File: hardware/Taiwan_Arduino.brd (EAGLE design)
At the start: 97.2 x 35.7 mm, 44 parts, among them J1 AVR_SPI_PRG_62X3_LOCK, T1 2SC, T2 2N, U1 ATMEGA328P_PDIP, Y2 16mhz

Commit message: Ver 1.0
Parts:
- removed T1: 2SC, transistor:TO92-ECB
- moved JP3 2.50 mm to (87.4, 23.5), turned to 180 degrees
- moved C1 2.35 mm to (77.4, 20.8)
- moved T2 1.61 mm to (83.2, 19.7)
- moved R16 0.61 mm to (75.5, 13.0)
- moved TP6 0.30 mm to (63.2, 9.83)
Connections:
- removed net N$18: JP3.2, T1.C, T2.C
- new net N$12: JP3.1, T2.C
- net +5V: now also JP3.2; no longer JP3.1
- net GND: no longer T1.E
- net N$22: no longer T1.B
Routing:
- net N$12: track 0.00 -> 6.79 mm
- net N$18: track 6.31 -> 0.00 mm
- net +5V: track 140.1 -> 144.2 mm
- net N$22: track 19.2 -> 22.6 mm
- net N$17: track 47.1 -> 48.2 mm
- net N$11: track 76.6 -> 76.0 mm
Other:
- board size 97.2 x 35.7 mm -> 97.4 x 35.6 mm

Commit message: ver 1.0
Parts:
- removed R7: 1M, SparkFun-Resistors:AXIAL-0.4
- removed TP5: TEST-POINT, SparkFun-Passives:PADBIG
- removed U$1: SPI_FLASH-X25XX, SparkFun-DigitalIC:DIL08
- added D3: 3.3V, _JJG-parts:0204V
- added JP1: Battery, SparkFun-Connectors:1X02
- added U2: SPI_FLASH, SparkFun-DigitalIC:DIL08
- C10, C13, C5, C8: device SparkFun-Capacitors:CAP-PTH-SMALL -> SparkFun-Capacitors:CAP-PTH-5MM
- C2: value 0.1uf -> 104; device SparkFun-Capacitors:CAP-PTH-SMALL -> SparkFun-Capacitors:CAP-PTH-5MM
- JP3: value M02JST-PTH-VERT -> M021X02_NO_SILK; device SparkFun-Connectors:JST-2-PTH-VERT -> SparkFun-Connectors:1X02_NO_SILK
- R1: value (none) -> 10
- R9: device SparkFun-Resistors:AXIAL-0.4 -> SparkFun-Resistors:AXIAL-0.1
- T2: value 2N -> 2N2222
- moved R8 10.2 mm to (70.1, 13.6)
- moved R9 7.37 mm to (26.0, 22.2), turned to 90 degrees
- moved C2 5.72 mm to (47.4, 9.20)
- moved JP3 4.26 mm to (86.0, 19.5), turned to 90 degrees
- moved R6 4.24 mm to (26.0, 16.9)
- moved U1 4.01 mm to (45.3, 21.0)
- moved R5 3.64 mm to (72.8, 13.6), turned to 270 degrees
- moved R10 2.80 mm to (32.7, 27.4)
- moved TP3 2.73 mm to (81.9, 11.3)
- moved R13 2.72 mm to (36.4, 14.5)
- moved RV1 2.62 mm to (69.2, 20.5)
- moved R12 2.60 mm to (38.9, 14.6)
- moved R11 2.53 mm to (44.5, 11.8)
- moved R15 2.50 mm to (34.9, 27.4), turned to 90 degrees
- moved C5 2.33 mm to (25.7, 13.4), turned to 0 degrees
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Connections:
- removed net N$27: R7.P$2, TP5.P$1, U1.6
- new net N$18: D3.1, JP1.2
- net +5V: now also D3.2, U2.3, U2.7, U2.8; no longer U$1.3, U$1.7, U$1.8
- net GND: now also JP1.1, U2.4; no longer U$1.4
- net N$10: now also U2.2; no longer U$1.2
- net N$11: now also U1.26; no longer R7.P$1, U1.25
- net N$23: now also U2.5; no longer U$1.5
- net N$28: now also U1.16, U2.1; no longer U$1.1, U1.14
- net N$3: now also U1.14; no longer U1.16
- net N$5: now also U1.25; no longer U1.24
- net N$6: now also U2.6; no longer U$1.6
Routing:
- net N$27: track 27.5 -> 0.00 mm
- net +5V: track 144.2 -> 159.4 mm
- net 1: track 11.9 -> 17.9 mm
- net N$17: track 48.2 -> 42.8 mm
- net N$3: track 35.4 -> 39.9 mm, vias 0 -> 1
- net N$13: track 14.0 -> 10.0 mm
- net N$18: track 0.00 -> 3.71 mm
- net N$11: track 76.0 -> 79.2 mm
- net N$9: track 10.7 -> 13.5 mm
- net N$12: track 6.79 -> 4.01 mm
- net N$15: track 17.1 -> 19.6 mm
- net N$5: track 14.9 -> 12.4 mm
- net N$14: track 10.7 -> 13.1 mm
- net N$2: track 7.57 -> 5.53 mm
- net N$29: track 31.7 -> 33.6 mm
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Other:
- board text added: "+"
- board text added: "-"
- board text added: "104"
- board text added: "22pf"
- board text added: "Bat"
- board text added: "Reset"
- board text added: "台灣"

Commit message: add tag on IO
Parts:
- moved TP8 0.98 mm to (90.4, 16.8)
- moved R10 0.30 mm to (32.4, 27.4)
- moved R15 0.20 mm to (34.7, 27.4)
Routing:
- net N$17: track 42.8 -> 43.4 mm
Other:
- board text added: "A2"
- board text added: "A4"
- board text added: "A5"
- board text added: "D5"
- board text added: "D6"
- board text added: "D8"
- board text removed: "台灣"

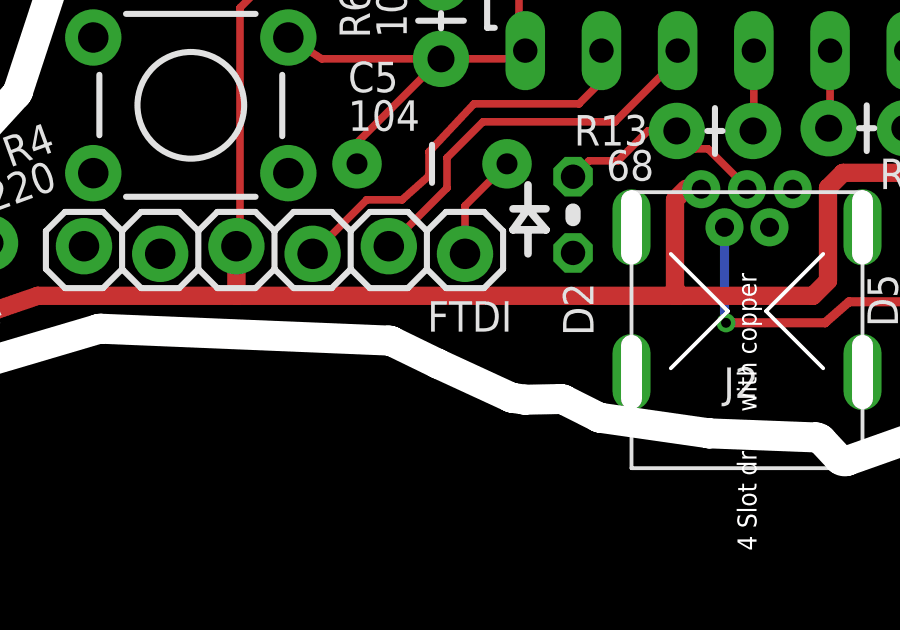
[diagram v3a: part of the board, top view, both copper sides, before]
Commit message: add tag on FTDI port
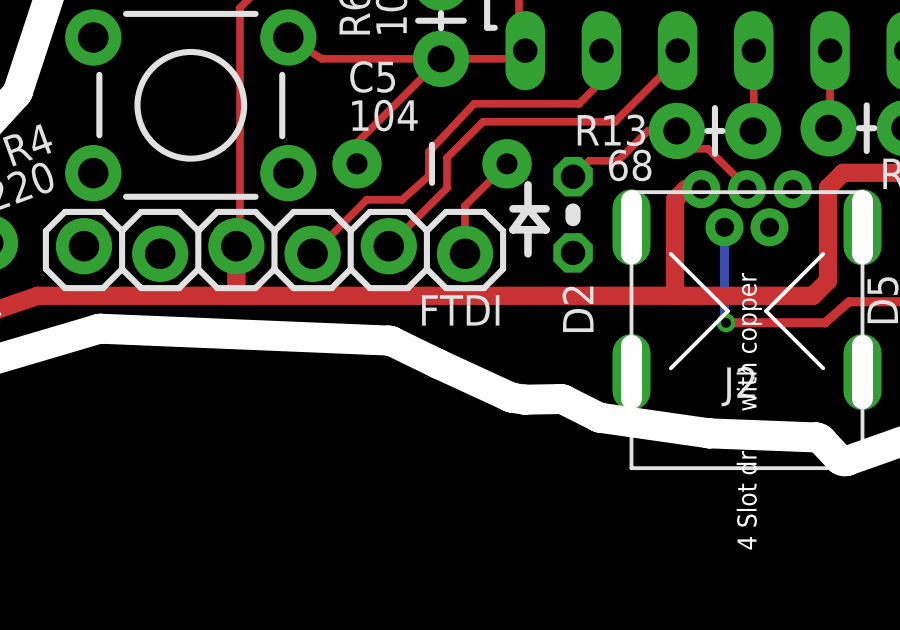
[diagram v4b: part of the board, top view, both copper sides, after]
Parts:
- FTDI: value (none) -> DTR
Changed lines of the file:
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@@
 <element name="TP8" library="SparkFun-Passives" package="PADBIG" value="TEST-POINT" x="90.375859375" y="16.8033125" rot="R200"/>
 <element name="TP9" library="SparkFun-Passives" package="PADBIG" value="TEST-POINT" x="80.3756375" y="27.159590625" rot="R200"/>
-<element name="FTDI" library="SparkFun-Connectors" package="1X06_LOCK" value="" x="26.8" y="10.4" smashed="yes" rot="R180">
-<attribute name="NAME" x="28.37" y="8.822" size="1.016" layer="25" font="vector" ratio="15" rot="R180"/>
-<attribute name="VALUE" x="28.07" y="13.702" size="1.27" layer="27" font="vector" rot="R180"/>
+<element name="FTDI" library="SparkFun-Connectors" package="1X06_LOCK" value="DTR" x="26.8" y="10.4" smashed="yes" rot="R180">
+<attribute name="NAME" x="28.07" y="9.022" size="1.016" layer="25" font="vector" ratio="15" rot="R180"/>
+<attribute name="VALUE" x="28.398" y="10.17" size="1.016" layer="27" font="vector" ratio="15" rot="R270"/>
 </element>
 <element name="RV1" library="SparkFun-Electromechanical" package="ALPS_POT" value="5k" x="69.229653125" y="20.472284375" smashed="yes" rot="R90">

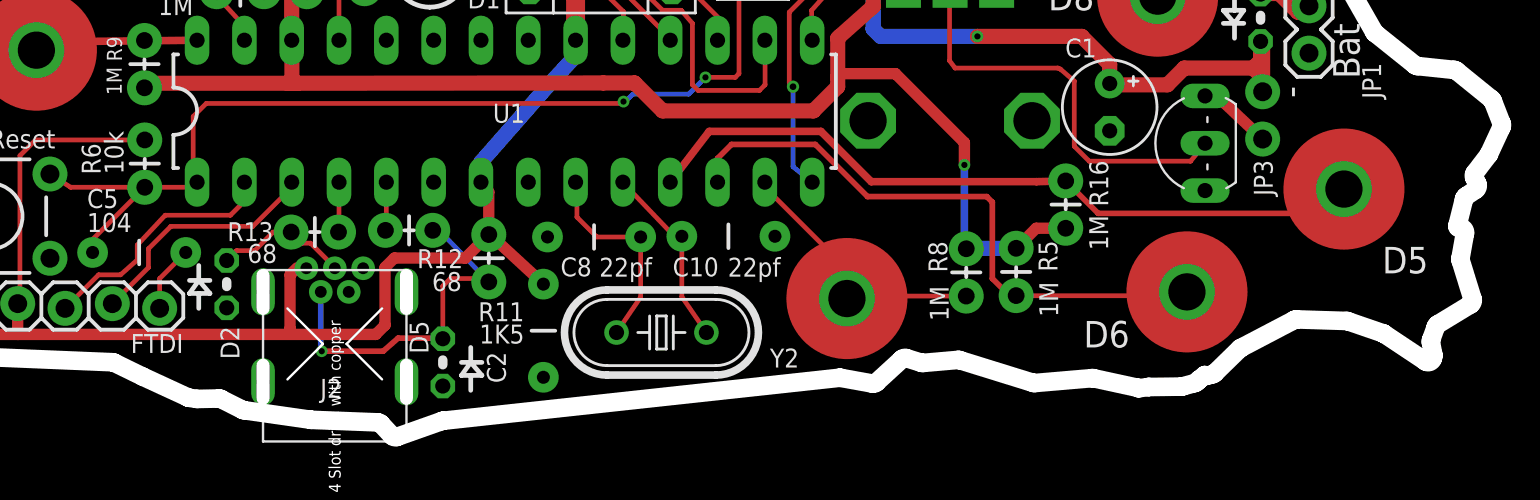
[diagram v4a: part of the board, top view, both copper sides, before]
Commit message: add tag on FTDI port
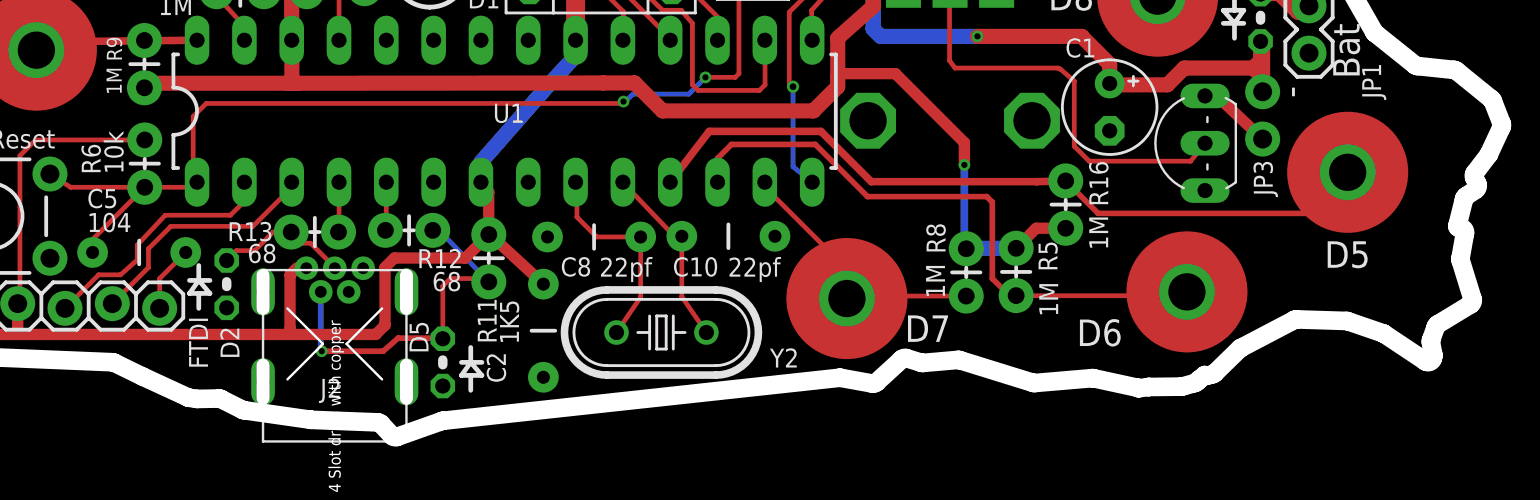
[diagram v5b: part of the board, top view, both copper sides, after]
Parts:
- moved TP8 0.92 mm to (90.6, 17.7)
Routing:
- net N$17: track 43.4 -> 42.6 mm
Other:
- board text added: "D7"
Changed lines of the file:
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@@
 <text x="42.2" y="30.3" size="1.4224" layer="21" font="vector" ratio="15">+</text>
 <text x="89.8" y="25.7" size="1.4224" layer="21" font="vector" ratio="15" rot="R270">Bat</text>
-<text x="94.9" y="13.7" size="1.4224" layer="21" font="vector" ratio="15" rot="R180">D5</text>
+<text x="91.8" y="14" size="1.4224" layer="21" font="vector" ratio="15" rot="R180">D5</text>
 <text x="50.4" y="12.1" size="1.016" layer="21" font="vector" ratio="15">22pf</text>
 <text x="57.3" y="12.1" size="1.016" layer="21" font="vector" ratio="15">22pf</text>
@@
 <text x="21.2" y="20" size="1.016" layer="21" font="vector" ratio="15" rot="R180">Reset</text>
 <text x="22.9" y="14.5" size="1.016" layer="21" font="vector" ratio="15">104</text>
-<text x="76.4" y="8.3" size="1.4224" layer="21" font="vector" ratio="15">D6</text>
+<text x="78.5" y="9.8" size="1.4224" layer="21" font="vector" ratio="15" rot="R180">D6</text>
 <text x="74.5" y="26.4" size="1.4224" layer="21" font="vector" ratio="15">D8</text>
 <text x="33.9" y="34.1" size="1.4224" layer="21" font="vector" ratio="15">A2</text>
 <text x="23.4" y="29.5" size="1.4224" layer="21" font="vector" ratio="15">A4</text>
 <text x="14.7" y="21.4" size="1.4224" layer="21" font="vector" ratio="15">A5</text>
+<text x="66.8" y="8.6" size="1.4224" layer="21" font="vector" ratio="15">D7</text>
 </plain>
 <attributes>
@@
 </element>
 <element name="R11" library="SparkFun-Resistors" package="AXIAL-0.1" value="1K5" x="44.469140625" y="11.821278125" smashed="yes" rot="R90">
-<attribute name="NAME" x="46.371921875" y="10.72485" size="1.016" layer="25" font="vector" ratio="15" rot="R180"/>
-<attribute name="VALUE" x="46.378721875" y="9.528140625" size="1.016" layer="21" font="vector" ratio="15" rot="R180"/>
+<attribute name="NAME" x="43.87515" y="10.971921875" size="1.016" layer="25" font="vector" ratio="15" rot="R270"/>
+<attribute name="VALUE" x="45.071859375" y="10.878721875" size="1.016" layer="21" font="vector" ratio="15" rot="R270"/>
 </element>
 <element name="R12" library="SparkFun-Resistors" package="AXIAL-0.1" value="68" x="38.92036875" y="14.587821875" smashed="yes">
@@
 <element name="TP4" library="SparkFun-Passives" package="PADBIG" value="TEST-POINT" x="20.183053125" y="24.260109375" rot="R290"/>
 <element name="TP6" library="SparkFun-Passives" package="PADBIG" value="TEST-POINT" x="63.69446875" y="10.9264875" rot="R290"/>
-<element name="TP8" library="SparkFun-Passives" package="PADBIG" value="TEST-POINT" x="90.375859375" y="16.8033125" rot="R200"/>
+<element name="TP8" library="SparkFun-Passives" package="PADBIG" value="TEST-POINT" x="90.575859375" y="17.7033125" rot="R200"/>
 <element name="TP9" library="SparkFun-Passives" package="PADBIG" value="TEST-POINT" x="80.3756375" y="27.159590625" rot="R200"/>
 <element name="FTDI" library="SparkFun-Connectors" package="1X06_LOCK" value="DTR" x="26.8" y="10.4" smashed="yes" rot="R180">
-<attribute name="NAME" x="28.07" y="9.022" size="1.016" layer="25" font="vector" ratio="15" rot="R180"/>
-<attribute name="VALUE" x="28.398" y="10.17" size="1.016" layer="27" font="vector" ratio="15" rot="R270"/>
+<attribute name="NAME" x="28.378" y="9.97" size="1.016" layer="25" font="vector" ratio="15" rot="R270"/>
+<attribute name="VALUE" x="27.97" y="9.102" size="1.016" layer="27" font="vector" ratio="15" rot="R180"/>
 </element>
 <element name="RV1" library="SparkFun-Electromechanical" package="ALPS_POT" value="5k" x="69.229653125" y="20.472284375" smashed="yes" rot="R90">
@@
 </element>
 <element name="R8" library="SparkFun-Resistors" package="AXIAL-0.1" value="1M" x="70.1" y="13.6" smashed="yes" rot="R270">
-<attribute name="NAME" x="68.07" y="14.000003125" size="1.016" layer="25" font="vector" ratio="15" rot="R270"/>
-<attribute name="VALUE" x="68.141003125" y="11.600003125" size="1.016" layer="21" font="vector" ratio="15" rot="R270"/>
+<attribute name="NAME" x="67.97" y="15.000003125" size="1.016" layer="25" font="vector" ratio="15" rot="R270"/>
+<attribute name="VALUE" x="67.941003125" y="12.800003125" size="1.016" layer="21" font="vector" ratio="15" rot="R270"/>
 </element>
 <element name="R9" library="SparkFun-Resistors" package="AXIAL-0.1" value="1M" x="25.98326875" y="22.240115625" smashed="yes" rot="R90">
@@
 <contactref element="TP8" pad="P$1"/>
 <wire x1="56.3" y1="19.9" x2="54.208196875" y2="17.17326875" width="0.4064" layer="1"/>
-<wire x1="90.375859375" y1="16.8033125" x2="90.8033125" y2="17.6033125" width="0.254" layer="1"/>
+<wire x1="90.575859375" y1="17.7033125" x2="90.8033125" y2="17.6033125" width="0.254" layer="1"/>
 <wire x1="91.1" y1="15.5" x2="77.178678125" y2="15.5" width="0.3048" layer="1"/>
 <wire x1="77.178678125" y1="15.5" x2="75.438746875" y2="17.23993125" width="0.3048" layer="1"/>
-<wire x1="91.1" y1="15.5" x2="91.2" y2="17.027453125" width="0.3048" layer="1"/>
-<wire x1="91.2" y1="17.027453125" x2="90.375859375" y2="16.8033125" width="0.3048" layer="1"/>
+<wire x1="91.1" y1="15.5" x2="90.7" y2="17.127453125" width="0.3048" layer="1"/>
+<wire x1="90.7" y1="17.127453125" x2="90.575859375" y2="17.7033125" width="0.3048" layer="1"/>
 <wire x1="62.3" y1="19.9" x2="56.3" y2="19.9" width="0.4064" layer="1"/>
 <wire x1="62.3" y1="19.9" x2="65" y2="17.2" width="0.4064" layer="1"/>
